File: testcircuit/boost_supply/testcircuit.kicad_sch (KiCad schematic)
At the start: 79 parts, among them P1 RZM001P02T2L, P10 RZM001P02T2L, P11 RZM001P02T2L, P12 RZM001P02T2L, P13 RZM001P02T2L, P14 RZM001P02T2L, P15 RZM001P02T2L, P16 RZM001P02T2L, P17 RZM001P02T2L, P18 RZM001P02T2L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

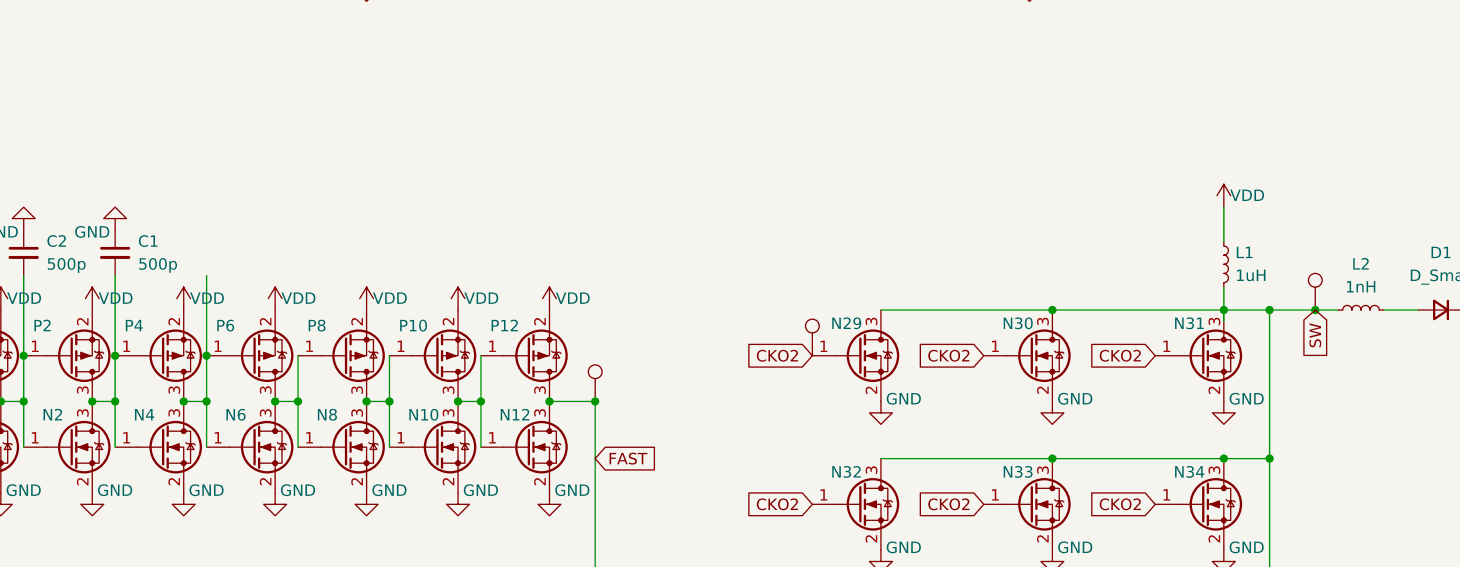
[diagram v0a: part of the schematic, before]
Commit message: add note about inductor
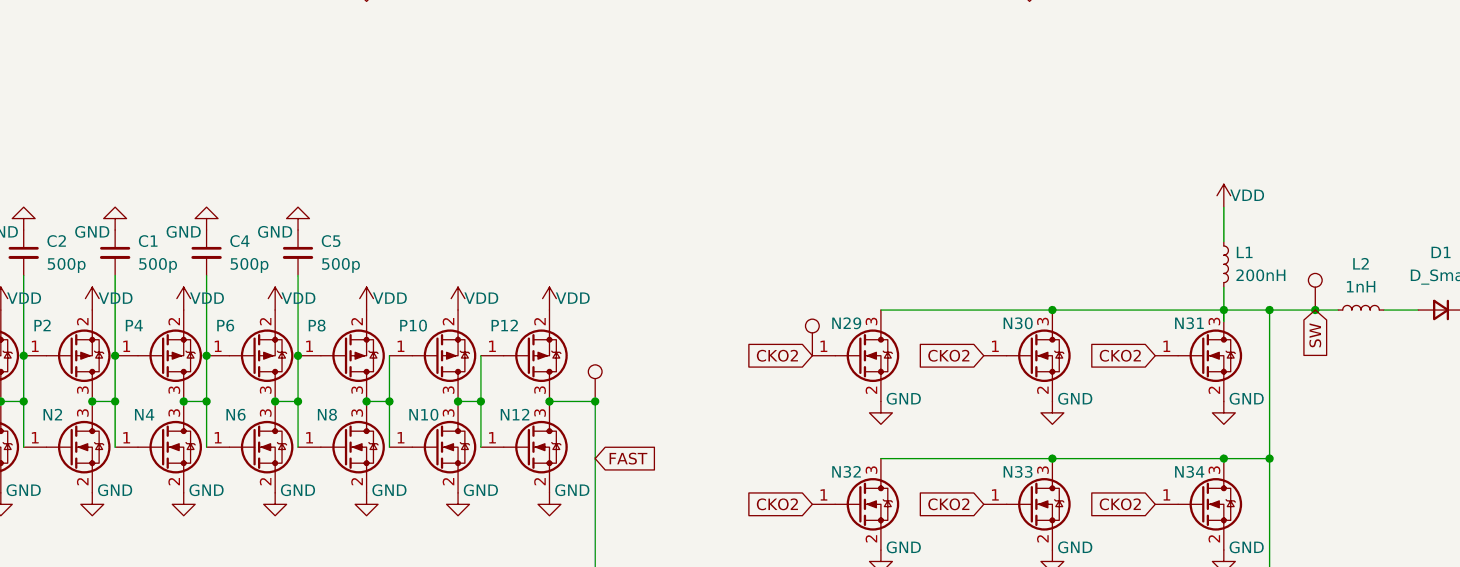
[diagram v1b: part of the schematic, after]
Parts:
- added C4, C5: 500p, symbol Device:C_Small
- L1: value 1uH -> 200nH
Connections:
- net GND: now also C4.1, C5.1
- net at N4.3 (D), N6.1 (G), P4.3 (D)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: now also C4.2
- net at N6.3 (D), N8.1 (G), P6.3 (D)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: now also C5.2
